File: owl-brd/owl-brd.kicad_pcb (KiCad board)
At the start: 2 copper layers, 99.1 x 86.4 mm, 60 parts, among them J1 JST, J10 JST, J11 JST, J12 JST, J13 Screw_Terminal_01x02, J14 1x4 Socket, J15 CLTCH1, J16 CLTCH2, J17 CLTCH3, J18 CLTCH4, J19 CLTCH5, J2 JST, J20 CLTCH6, J21 CLTCH7, J22 CLTCH1, J23 Conn_01x03, J24 Conn_01x03, J25 Conn_01x03, J26 Conn_01x03, J27 Screw_Terminal_01x02, J28 JST, J29 Ext Power, J3 JST, J30 Power/UART, J4 JST, J5 JST, J6 JST, J7 JST, J8 JST, J9 JST, Q9 IRLB8721PBF, U1 Pico, U2 L7805CV, U3 TMC2209_SILENTSTEPSTICK, U4 TMC2209_SILENTSTEPSTICK, U5 TMC2209_SILENTSTEPSTICK, U6 TCA9548APWR, U7 74HC238, U8 ULN2803A

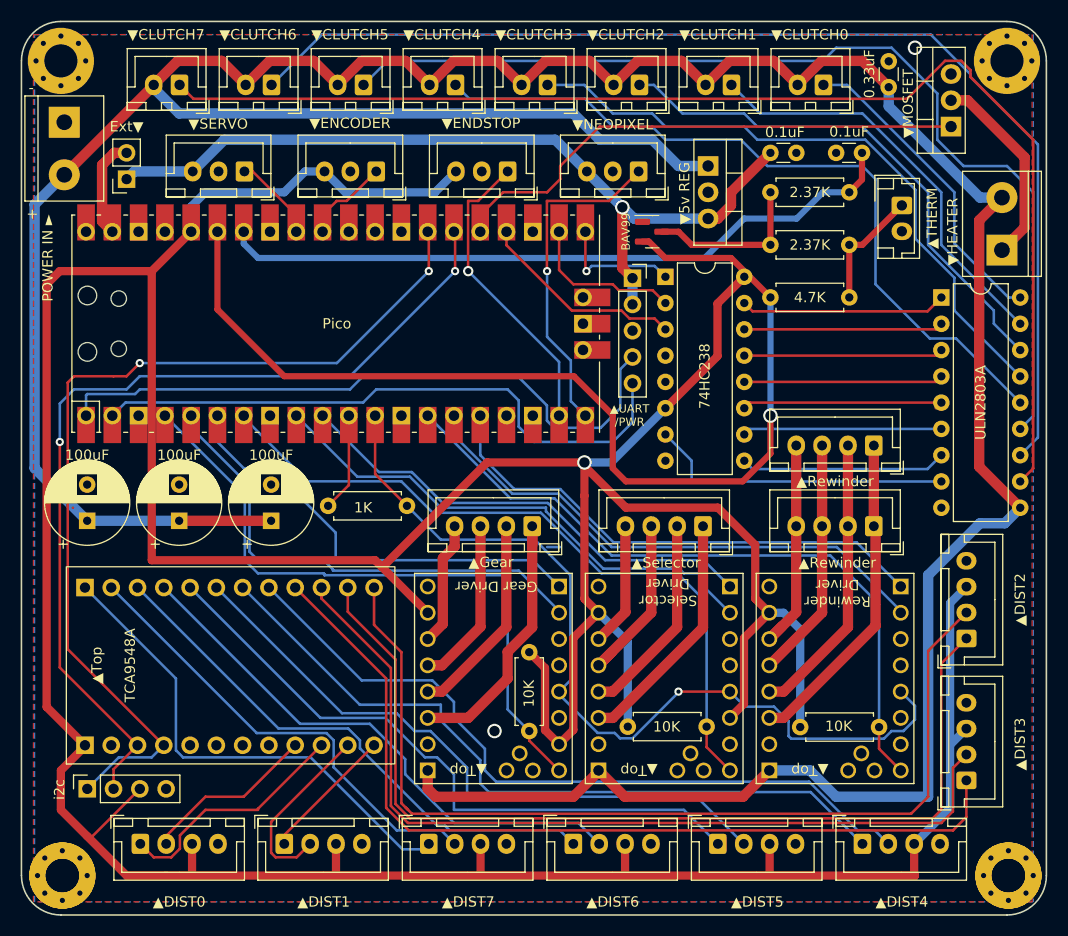
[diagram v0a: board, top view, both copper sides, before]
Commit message: - Fix for thermistor mixing vref with 3v3 - Fix footprint for thermistor JST connector - Added enable pin for decoder so that one clutch doesn't have to be on all the time - TODO: rework the CLUTCH pins thickness -- the current thickness may be resulting in a voltage drop and not be sufficient for current
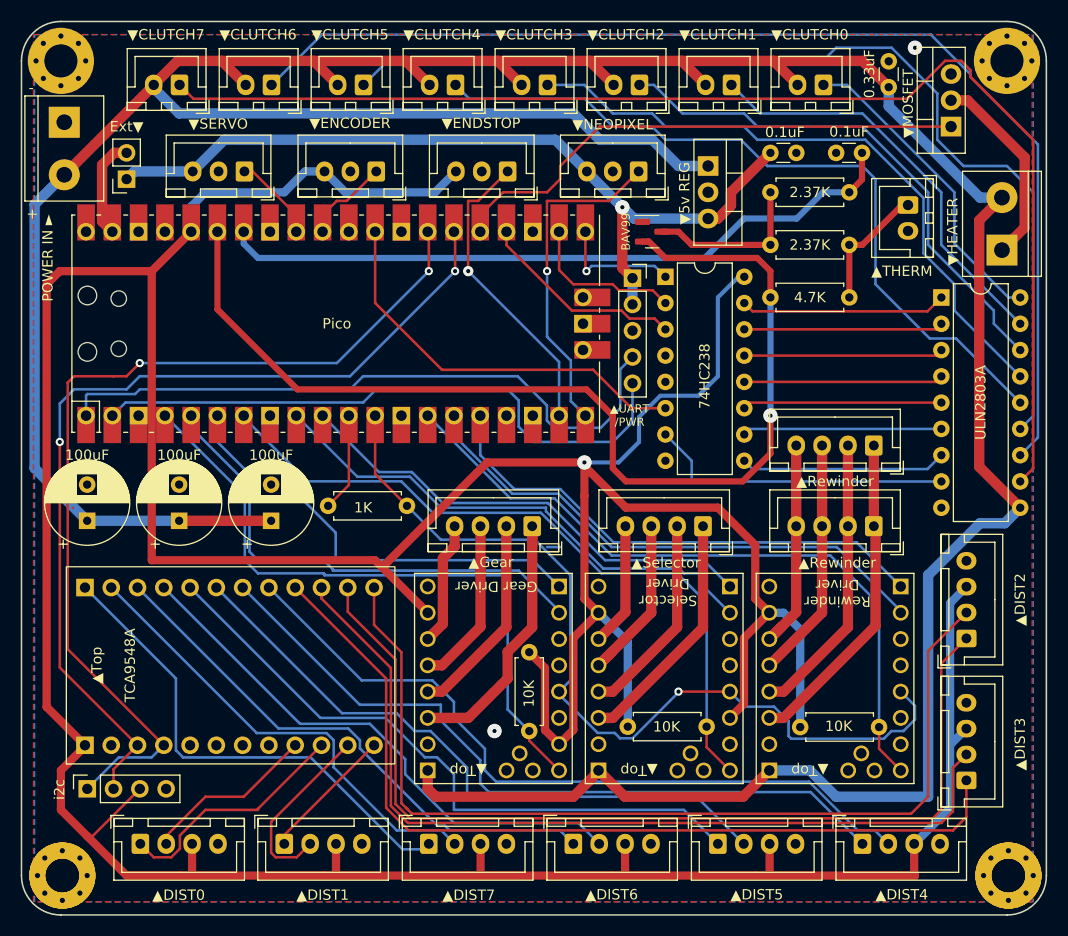
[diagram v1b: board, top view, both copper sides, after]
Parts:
- J28: footprint Connector_JST:JST_EH_B2B-EH-A_1x02_P2.50mm_Vertical -> Connector_JST:JST_XH_B2B-XH-A_1x02_P2.50mm_Vertical
- moved J28 0.59 mm to (98.4, 31.7)
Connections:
- U1 pad 29: unconnected-(U1-Pad29) -> CLTCH_EN
- U7 pad 6: +3V3 -> CLTCH_EN
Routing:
- net CLTCH_EN: track 0.00 -> 39.2 mm
- net +24V: track 347.4 -> 356.9 mm
- net +3V3: track 450.1 -> 453.5 mm
- net ADC_VREF: track 101.7 -> 103.2 mm
- net Net-(J28-Pad1): track 11.7 -> 12.3 mm

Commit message: -3d models/images -Flipped mosfet -Changed UART order (and labels to match pico rx/tx), in line with Pi and SKR headers
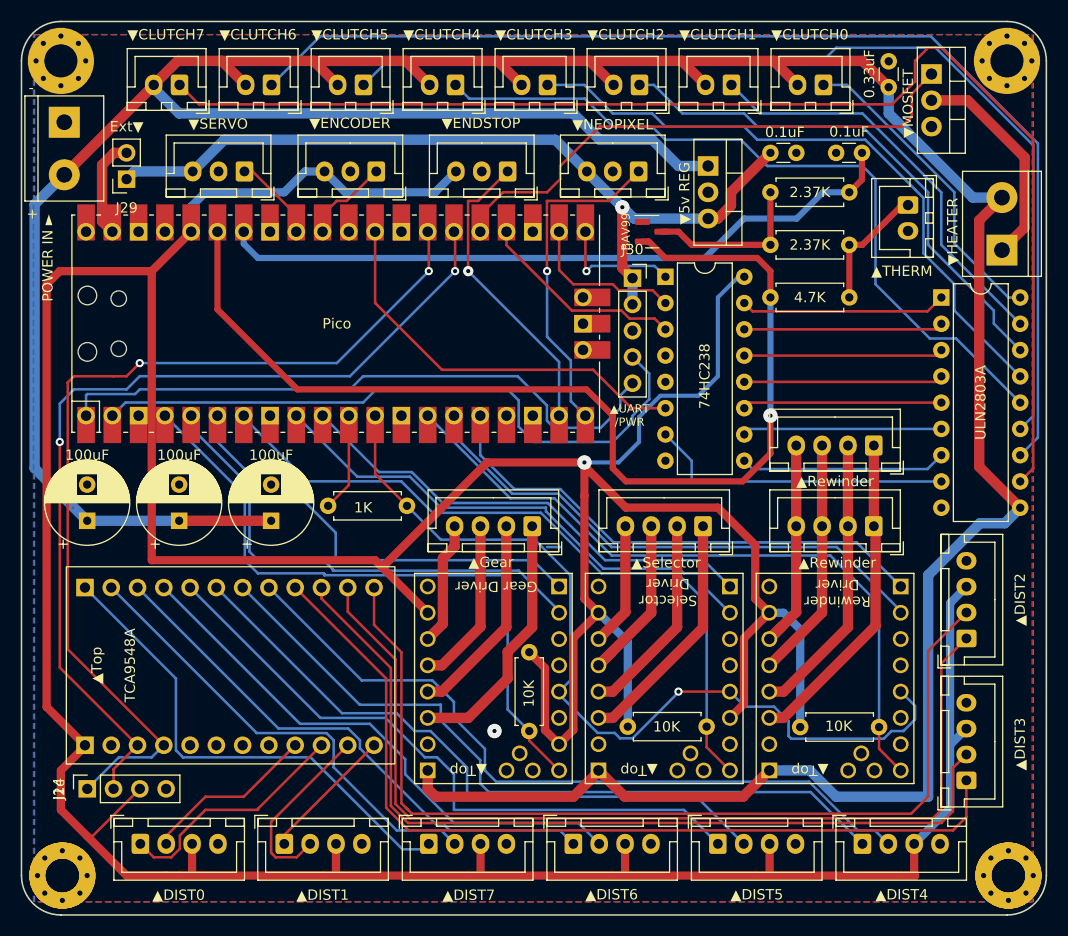
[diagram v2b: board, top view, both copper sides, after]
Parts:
- moved Q9 5.42 mm to (100.7, 19.1), turned to -90 degrees
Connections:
- U1 pad 1: RX -> TX
- U1 pad 2: TX -> RX
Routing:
- net Net-(J22-Pad1): track 121.9 -> 124.2 mm
- net Net-(J27-Pad1): track 19.5 -> 21.4 mm
- net HEATER: track 53.0 -> 54.5 mm
- net RX: track 63.5 -> 65.0 mm
- net GND: vias 2 -> 1
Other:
- board text added: "DRAIN"
- board text added: "GATE"

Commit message: Revision 1.0.1 - Removed 5v on UART pins (output isn't enough for pi) - Notes/minor cleanup for production
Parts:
- J14: footprint Connector_PinSocket_2.54mm:PinSocket_1x04_P2.54mm_Vertical -> Connector_PinHeader_2.54mm:PinHeader_1x04_P2.54mm_Vertical
- J23: value Conn_01x03 -> Encoder
- J24: value Conn_01x03 -> Endstop
- J25: value Conn_01x03 -> Servo
- J26: value Conn_01x03 -> Neopixel/Misc
- J29: footprint Connector_PinSocket_2.54mm:PinSocket_1x02_P2.54mm_Vertical -> Connector_PinHeader_2.54mm:PinHeader_1x02_P2.54mm_Vertical
- J30: value Power/UART -> UART; footprint Connector_PinSocket_2.54mm:PinSocket_1x05_P2.54mm_Vertical -> Connector_PinHeader_2.54mm:PinHeader_1x03_P2.54mm_Vertical
- moved J30 5.18 mm to (71.8, 44.0)
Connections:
- J30 pad 1: +5V -> GND
- J30 pad 2: +5V -> RX
- J30 pad 3: GND -> TX
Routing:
- net +5V: track 82.1 -> 70.7 mm, vias 1 -> 0
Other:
- board text added: "OwlBrd v1.0.1 ©2022 Alexander Nagelberg"
- board text added: "▲UART"
- board text removed: "OwlBrd v1.0 ©2022 Alexander Nagelberg"
- board text removed: "▲UART /PWR"
